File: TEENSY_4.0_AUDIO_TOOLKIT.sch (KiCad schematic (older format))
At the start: 46 parts, among them J1 MIDI_IO1, J14 USB_A, U3 Teensy4.0, U4C1 22 uF, U4C2 0.47uF, U4C3 0.47uF, U4C4 22 uF

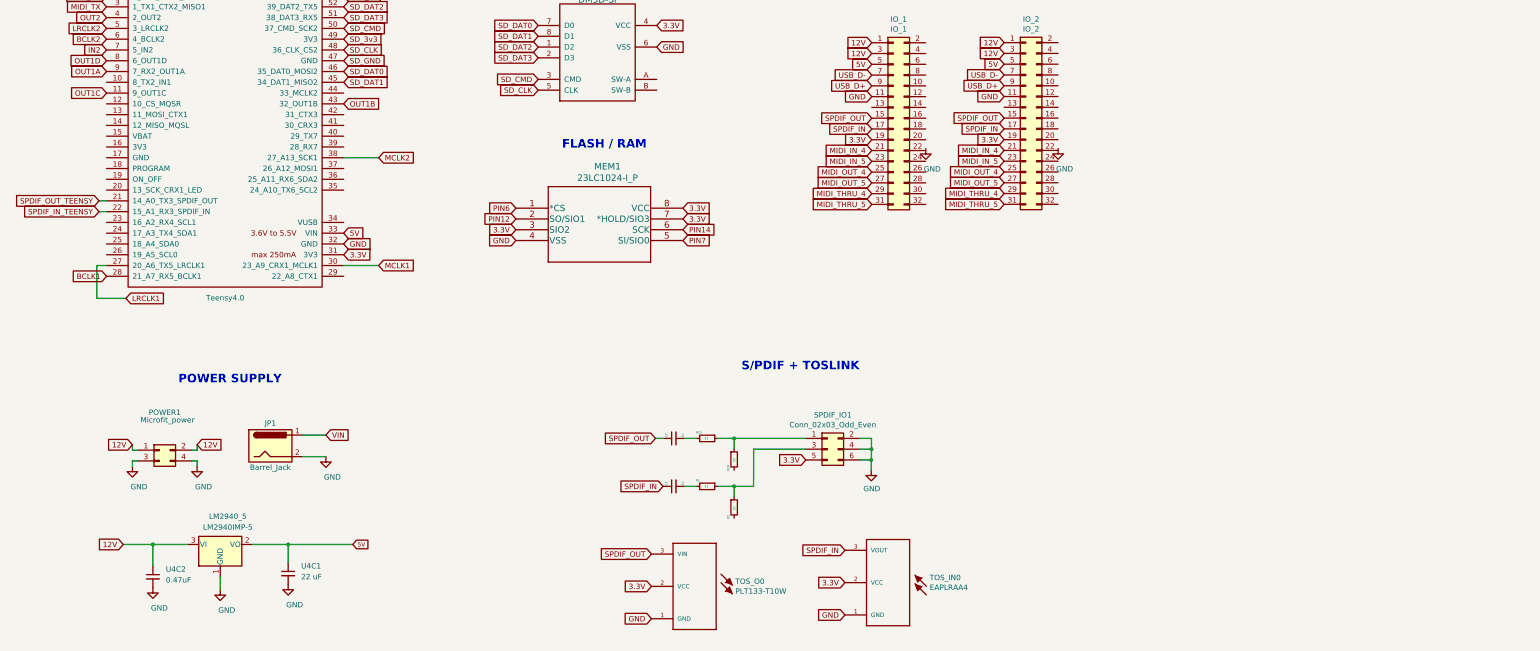
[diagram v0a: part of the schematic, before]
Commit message: Added SAI Expansion Headers
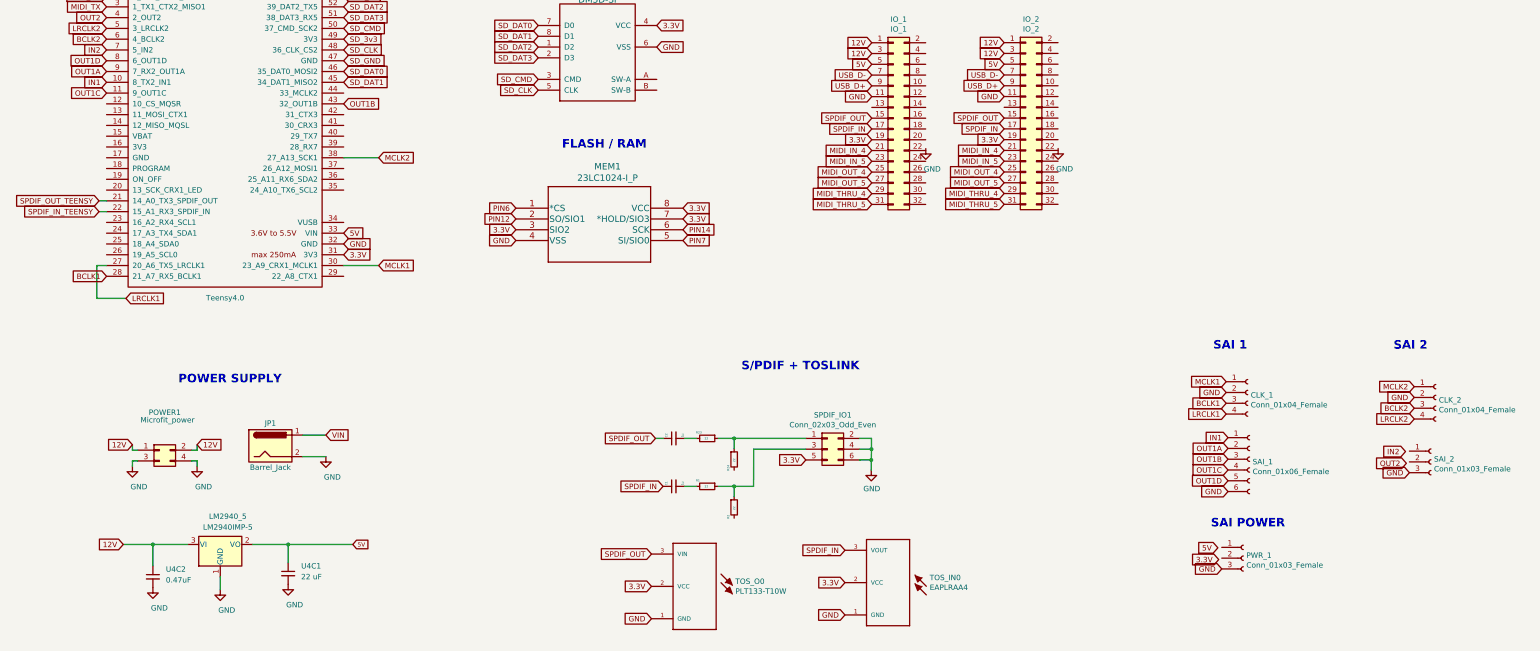
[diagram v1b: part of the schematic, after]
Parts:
- added CLK_1, CLK_2: Conn_01x04_Female, Connector_PinSocket_2.54mm:PinSocket_1x04_P2.54mm_Vertical, symbol Connector:Conn_01x04_Female
- added PWR_1, SAI_2: Conn_01x03_Female, Connector_PinSocket_2.54mm:PinSocket_1x03_P2.54mm_Vertical, symbol Connector:Conn_01x03_Female
- added SAI_1: Conn_01x06_Female, Connector_PinSocket_2.54mm:PinSocket_1x06_P2.54mm_Vertical, symbol Connector:Conn_01x06_Female
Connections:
- net BCLK1: now also CLK_1.3 (Pin_3)
- net BCLK2: now also CLK_2.3 (Pin_3)
- net GND: now also CLK_1.2 (Pin_2), CLK_2.2 (Pin_2), PWR_1.3 (Pin_3), SAI_1.6 (Pin_6), SAI_2.3 (Pin_3)
- net LRCLK1: now also CLK_1.4 (Pin_4)
- net LRCLK2: now also CLK_2.4 (Pin_4)
- net MCLK1: now also CLK_1.1 (Pin_1)
- net MCLK2: now also CLK_2.1 (Pin_1)
- net OUT1A: now also SAI_1.2 (Pin_2)
- net OUT1B: now also SAI_1.3 (Pin_3)
- net OUT1C: now also SAI_1.4 (Pin_4)
- net OUT1D: now also SAI_1.5 (Pin_5)
- net IN1: now reaches U3.10 (8_TX2_IN1)
- net IN1: now also SAI_1.1 (Pin_1)
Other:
- note added: "SAI 1"
- note added: "SAI 2"
- note added: "SAI POWER"
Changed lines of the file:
@@
 Text Notes 9888 2140 0    79   ~ 16
 IO HEADER
+Text Notes 11933 5482 0    79   ~ 16
+SAI 1
+$Comp
+L Connector:Conn_01x04_Female CLK_1
+U 1 1 5E93116A
+P 12253 5870
+F 0 "CLK_1" H 12281 5846 50  0000 L CNN
+F 1 "Conn_01x04_Female" H 12281 5755 50  0000 L CNN
+F 2 "Connector_PinSocket_2.54mm:PinSocket_1x04_P2.54mm_Vertical" H 12253 5870 50  0001 C CNN
+F 3 "~" H 12253 5870 50  0001 C CNN
+	1    12253 5870
+	1    0    0    -1
+$EndComp
+Text GLabel 13798 6016 0    50   Input ~ 0
+BCLK2
+Text GLabel 13798 6116 0    50   Input ~ 0
+LRCLK2
+Text GLabel 12053 5970 0    50   Input ~ 0
+BCLK1
+Text GLabel 13798 5816 0    50   Input ~ 0
+MCLK2
+Text GLabel 12053 5770 0    50   Input ~ 0
+MCLK1
+Text GLabel 12053 6070 0    50   Input ~ 0
+LRCLK1
+$Comp
+L Connector:Conn_01x04_Female CLK_2
+U 1 1 5E959A09
+P 13998 5916
+F 0 "CLK_2" H 14026 5892 50  0000 L CNN
+F 1 "Conn_01x04_Female" H 14026 5801 50  0000 L CNN
+F 2 "Connector_PinSocket_2.54mm:PinSocket_1x04_P2.54mm_Vertical" H 13998 5916 50  0001 C CNN
+F 3 "~" H 13998 5916 50  0001 C CNN
+	1    13998 5916
+	1    0    0    -1
+$EndComp
+Text GLabel 12053 5870 0    50   Input ~ 0
+GND
+Text GLabel 13798 5916 0    50   Input ~ 0
+GND
+$Comp
+L Connector:Conn_01x03_Female SAI_2
+U 1 1 5E9CE1C2
+P 13953 6514
+F 0 "SAI_2" H 13981 6540 50  0000 L CNN
+F 1 "Conn_01x03_Female" H 13981 6449 50  0000 L CNN
+F 2 "Connector_PinSocket_2.54mm:PinSocket_1x03_P2.54mm_Vertical" H 13953 6514 50  0001 C CNN
+F 3 "~" H 13953 6514 50  0001 C CNN
+	1    13953 6514
+	1    0    0    -1
+$EndComp
+Text GLabel 1665 2992 0    50   Input ~ 0
+IN1
+Text GLabel 12070 6489 0    50   Input ~ 0
+OUT1B
+Text GLabel 12070 6389 0    50   Input ~ 0
+OUT1A
+Text GLabel 12070 6689 0    50   Input ~ 0
+OUT1D
+Text GLabel 13725 6527 0    50   Input ~ 0
+OUT2
+Text GLabel 13717 6418 0    50   Input ~ 0
+IN2
+Text GLabel 12070 6289 0    50   Input ~ 0
+IN1
+Text GLabel 12070 6589 0    50   Input ~ 0
+OUT1C
+Text GLabel 13753 6614 0    50   Input ~ 0
+GND
+Text GLabel 12070 6789 0    50   Input ~ 0
+GND
+$Comp
+L Connector:Conn_01x06_Female SAI_1
+U 1 1 5EA54A02
+P 12270 6489
+F 0 "SAI_1" H 12298 6465 50  0000 L CNN
+F 1 "Conn_01x06_Female" H 12298 6374 50  0000 L CNN
+F 2 "Connector_PinSocket_2.54mm:PinSocket_1x06_P2.54mm_Vertical" H 12270 6489 50  0001 C CNN
+F 3 "~" H 12270 6489 50  0001 C CNN
+	1    12270 6489
+	1    0    0    -1
+$EndComp
+$Comp
+L Connector:Conn_01x03_Female PWR_1
+U 1 1 5EAACE2F
+P 12212 7407
+F 0 "PWR_1" H 12240 7433 50  0000 L CNN
+F 1 "Conn_01x03_Female" H 12240 7342 50  0000 L CNN
+F 2 "Connector_PinSocket_2.54mm:PinSocket_1x03_P2.54mm_Vertical" H 12212 7407 50  0001 C CNN
+F 3 "~" H 12212 7407 50  0001 C CNN
+	1    12212 7407
+	1    0    0    -1
+$EndComp
+Text GLabel 11984 7420 0    50   Input ~ 0
+3.3V
+Text GLabel 11976 7311 0    50   Input ~ 0
+5V
+Text GLabel 12012 7507 0    50   Input ~ 0
+GND
+Text Notes 13606 5483 0    79   ~ 16
+SAI 2
+Text Notes 11911 7132 0    79   ~ 16
+SAI POWER
 $EndSCHEMATC

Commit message: Update
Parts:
- removed CLK_1, CLK_2: Conn_01x04_Female, Connector_PinSocket_2.54mm:PinSocket_1x04_P2.54mm_Vertical, symbol Connector:Conn_01x04_Female
- removed IO_1: IO_1, Connector_PinHeader_2.54mm:PinHeader_2x15_P2.54mm_Vertical, symbol Connector_Generic:Conn_02x16_Odd_Even
- removed IO_2: IO_2, Connector_PinHeader_2.54mm:PinHeader_2x15_P2.54mm_Vertical, symbol Connector_Generic:Conn_02x16_Odd_Even
- removed J1: MIDI_IO1, Connector_PinHeader_2.54mm:PinHeader_2x06_P2.54mm_Vertical, symbol Connector_Generic:Conn_02x06_Odd_Even
- removed J14: USB_A, TE_USB_A_USBA_292303-4:TE_292303-4, symbol Connector:USB_A
- removed JP1: Barrel_Jack, Connector_BarrelJack:BarrelJack_CUI_PJ-063AH_Horizontal, symbol Connector:Barrel_Jack
- removed MIDI_IN_1, MIDI_OUT_1, MIDI_THROUGH_1: DIN-5, project_fp:SDS-50J_MIDI_JACK, symbol Connector:DIN-5
- removed MIDI_IN_2, MIDI_OUT_2, MIDI_THROUGH_2: 35RAPC4BHN2, project_fp:3.5MM_SWITCHCRAFT_35RAPC4BHN2, symbol 35RAPC4BHN2:35RAPC4BHN2
- removed POWER1: Microfit_power, Connector_Molex:Molex_Micro-Fit_3.0_43045-0412_2x02_P3.00mm_Vertical, symbol Connector_Generic:Conn_02x02_Odd_Even
- removed PWR_1, SAI_2: Conn_01x03_Female, Connector_PinSocket_2.54mm:PinSocket_1x03_P2.54mm_Vertical, symbol Connector:Conn_01x03_Female
- removed SAI_1: Conn_01x06_Female, Connector_PinSocket_2.54mm:PinSocket_1x06_P2.54mm_Vertical, symbol Connector:Conn_01x06_Female
- removed SD1: DM3D-SF, DM3D-SF:DM3D-SF, symbol TEENSY_4.0_AUDIO_BREAKOUT-rescue:DM3D-SF-Hirose
- removed SPDIF_IN1, SPDIF_OUT0: PJRAN1X1U04X, project_fp:SPDIF_PJRAN1X1U01X, symbol SPDIF_PJRAN1X1U04X:PJRAN1X1U04X
- removed TOS_IN0: EAPLRAA4, PLR135-T10_PLT133-T10W, symbol EAPLRAA4:EAPLRAA4
- removed TOS_O0: PLT133-T10W, PLT133-T10W:PLR135-T10_PLT133-T10W, symbol PLT133-T10W:PLT133-T10W
- removed TPS2055A_1: TPS2055A, Package_SO:SOIC-8_3.9x4.9mm_P1.27mm, symbol TEENSY_4.0_AUDIO_BREAKOUT-rescue:TPS2055A-TPS2055A
- removed USB_IO1: USB_Header, Connector_PinHeader_2.54mm:PinHeader_1x05_P2.54mm_Vertical, symbol TEENSY_4.0_AUDIO_BREAKOUT-rescue:USB_Header_5_Pin-USB_Header
- added IO_1: IO_1, project_fp:PinHeader_2x18_P2.54mm_Vertical, symbol Connector_Generic:Conn_02x18_Odd_Even
- added MCLK1: MCLK1, project_fp:SolderWirePad_1x01_THROUGH_SOLDER, symbol Connector:Conn_01x01_Male
- added MCLK2: MCLK2, project_fp:SolderWirePad_1x01_THROUGH_SOLDER, symbol Connector:Conn_01x01_Male
- added MIDI_IO1: MIDI_IO1, project_fp:PinHeader_2x06_P2.54mm_Vertical, symbol Connector_Generic:Conn_02x06_Odd_Even
- added POWER_IN1, POWER_OUT1: Conn_02x02_Odd_Even, project_fp:PinHeader_2x02_P2.54mm_Vertical, symbol Connector_Generic:Conn_02x02_Odd_Even
- added R10, R11: 2.2K, Resistor_SMD:R_0603_1608Metric_Pad1.05x0.95mm_HandSolder, symbol Device:R_Small
- added R12, R4: 100 Ohm, Resistor_SMD:R_0603_1608Metric_Pad1.05x0.95mm_HandSolder, symbol Device:R_Small
- added R3: 220R, Resistor_SMD:R_0603_1608Metric_Pad1.05x0.95mm_HandSolder, symbol Device:R_Small
- added SD1: DM3D-SF-Hirose, project_fp:DM3D-SF, symbol lib_sch:lib_sch_DM3D-SF-Hirose
- added TPS2055A_1: TPS2055A-TPS2055A, project_fp:SOIC-8_3.9x4.9mm_P1.27mm, symbol lib_sch:lib_sch_TPS2055A-TPS2055A
- added USB_IO1: USB_Header_5_Pin-USB_Header, project_fp:PinHeader_1x05_P2.54mm_Vertical, symbol lib_sch:lib_sch_USB_Header_5_Pin-USB_Header
- 6N137_1: footprint Package_DIP:DIP-8_W7.62mm_SMDSocket_SmallPads -> project_fp:DIP-8_W7.62mm_SMDSocket_SmallPads
- MEM1: footprint project_fp:23LC1024-I&slash_ST -> project_fp:23LC1024
- SPDIF_IO1: footprint Connector_PinHeader_2.54mm:PinHeader_2x03_P2.54mm_Vertical -> project_fp:PinHeader_2x03_P2.54mm_Vertical
- U3: footprint teensy:Teensy40_SMT -> project_fp:Teensy40_SMT_Audio_Kit_2
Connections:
- net labels added: 5V_TPS2055A, 5V_TPS2055A_H, GND_H, MIDI_IN_4_H, MIDI_IN_5_H, MIDI_OUT_4_H, MIDI_OUT_5_H, MIDI_THRU_4_H, MIDI_THRU_5_H, SCL0, SDA0, SPDIF_3.3V, SPDIF_3.3V_H, SPDIF_IN_H, SPDIF_OUT_H, USB_D+_H, USB_D-_H
- wire segments 123 -> 115
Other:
- note added: "CONNECTORS"
- note added: "I2C PULL UP"
- note added: "MASTER CLOCKS"
- note added: "MIDI HEADER"
- note removed: "3 PIN MIDI"
- note removed: "SAI 1"
- note removed: "SAI 2"
- note removed: "SAI POWER"
- moved on the sheet: 6N137_1, 74LS0A, 74LS0B, 74LS0C, 74LS0D, 74LS0E, C9, D1, LM2940_3, LM2940_5, R38, R5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

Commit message: Update
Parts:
- added C3: .1 uF, Capacitor_SMD:C_0603_1608Metric, symbol Device:C_Small
- added R13: 470, Resistor_SMD:R_0603_1608Metric_Pad1.05x0.95mm_HandSolder, symbol Device:R_Small
- R6, R9: value 47 -> 220
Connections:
- net labels added: 12V_H, 3.3V_H, 3.3v, 5V_H
- wire segments 115 -> 112
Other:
- moved on the sheet: 6N137_1, 74LS0A, 74LS0B, 74LS0C, 74LS0D, 74LS0E, C1, C2, D1, LM2940_3, MIDI_IO1, R1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
